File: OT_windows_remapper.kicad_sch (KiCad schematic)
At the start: 68 parts, among them J5 ICSP, Q1 BC547, Q10 BC547, Q2 BC547, Q3 BC547, Q4 BC558, Q5 BC558, Q6 BC558, Q7 BC558, Q8 BC558, Q9 BC558, U1 ATmega328P-P, U2 L7805, Y1 16M

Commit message: First routing
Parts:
- removed C7: 100n, Capacitor_THT:C_Rect_L7.0mm_W2.5mm_P5.00mm, symbol Device:C
- removed J15, J2: (no value), symbol Connector:Screw_Terminal_01x02
- removed J16: (no value), symbol Connector:Screw_Terminal_01x03
- added J15, J2, J4: 12Vdc, Connector_Wire:SolderWire-2sqmm_1x01_D2mm_OD3.9mm, symbol Connector:Screw_Terminal_01x01
- added J16: (no value), Connector_Wire:SolderWire-0.75sqmm_1x01_D1.25mm_OD2.3mm, symbol Connector:Screw_Terminal_01x01
- added J17: GND, Connector_Wire:SolderWire-0.75sqmm_1x01_D1.25mm_OD2.3mm, symbol Connector:Screw_Terminal_01x01
- added J18, J19: (no value), Connector_Wire:SolderWire-2sqmm_1x01_D2mm_OD3.9mm, symbol Connector:Screw_Terminal_01x01
- D1, D2, D3, D4, D5, D6, D7: footprint (none) -> Diode_THT:D_DO-41_SOD81_P2.54mm_Vertical_KathodeUp
- J1: value (none) -> Vcc_in
- J10: value (none) -> Down_IN; footprint (none) -> Connector_Wire:SolderWire-0.75sqmm_1x01_D1.25mm_OD2.3mm
- J11: value (none) -> Up_IN; footprint (none) -> Connector_Wire:SolderWire-0.75sqmm_1x01_D1.25mm_OD2.3mm
- J12: value (none) -> Up_REM; footprint (none) -> Connector_Wire:SolderWire-0.75sqmm_1x01_D1.25mm_OD2.3mm
- J13: value (none) -> Down_REM; footprint (none) -> Connector_Wire:SolderWire-0.75sqmm_1x01_D1.25mm_OD2.3mm
- J14: value (none) -> CClose_IN; footprint (none) -> Connector_Wire:SolderWire-0.75sqmm_1x01_D1.25mm_OD2.3mm
- J3: value (none) -> EPSW_aux; footprint (none) -> Connector_Wire:SolderWire-0.75sqmm_1x02_P4.8mm_D1.25mm_OD2.3mm
- J6: value (none) -> Up_OUT; footprint (none) -> Connector_Wire:SolderWire-0.75sqmm_1x01_D1.25mm_OD2.3mm
- J7: value (none) -> Down_OUT; footprint (none) -> Connector_Wire:SolderWire-0.75sqmm_1x01_D1.25mm_OD2.3mm
- J8: value (none) -> Auth_OUT; footprint (none) -> Connector_Wire:SolderWire-0.75sqmm_1x01_D1.25mm_OD2.3mm
- J9: value (none) -> Auth_IN; footprint (none) -> Connector_Wire:SolderWire-0.75sqmm_1x01_D1.25mm_OD2.3mm
- R1, R10, R11, R12, R13, R14, R15, R16, R17, R18, R19, R2, R20, R21, R22, R23, R24, R25, R26, R3, R4, R5, R6, R7, R8, R9: footprint (none) -> Resistor_THT:R_Axial_DIN0207_L6.3mm_D2.5mm_P2.54mm_Vertical
- U2: footprint Package_TO_SOT_THT:TO-220-3_Horizontal_TabDown -> (none)
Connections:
- net GND: now also J5.1 (Pin_1), J16.1 (Pin_1), J17.1 (Pin_1), J18.1 (Pin_1), J19.1 (Pin_1); no longer J5.5 (Pin_5)
- net at C4.1, C5.1, J3.2 (Pin_2)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: no longer C6.1
- net at Q7.1 (C), R22.1: now also U1.5 (PD3); no longer U1.13 (PD7)
- net at Q5.1 (C), R20.1: now also U1.14 (PB0); no longer U1.24 (PC1)
- net at Q6.1 (C), R21.1: now also U1.15 (PB1); no longer U1.23 (PC0)
- net at U1.1 (~{RESET}/PC6): now also J5.5 (Pin_5); no longer J5.1 (Pin_1)
- net at J5.2 (Pin_2), U1.17 (PB3): no longer R25.1
- net at R13.1: now also U1.4 (PD2); no longer U1.14 (PB0)
- net at R12.1: now also U1.3 (PD1); no longer U1.15 (PB1)
- net at U1.16 (PB2): now also R25.1; no longer R11.1
- net at U1.2 (PD0): now also R11.1
- net at Q4.1 (C), R19.1: now also U1.6 (PD4); no longer U1.25 (PC2)
- net at C3.1, J1.1 (Pin_1), U2.1 (IN): now also C6.1
- new net: J15.1 (Pin_1), J2.1 (Pin_1), J4.1 (Pin_1)
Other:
- moved on the sheet: C6, U2

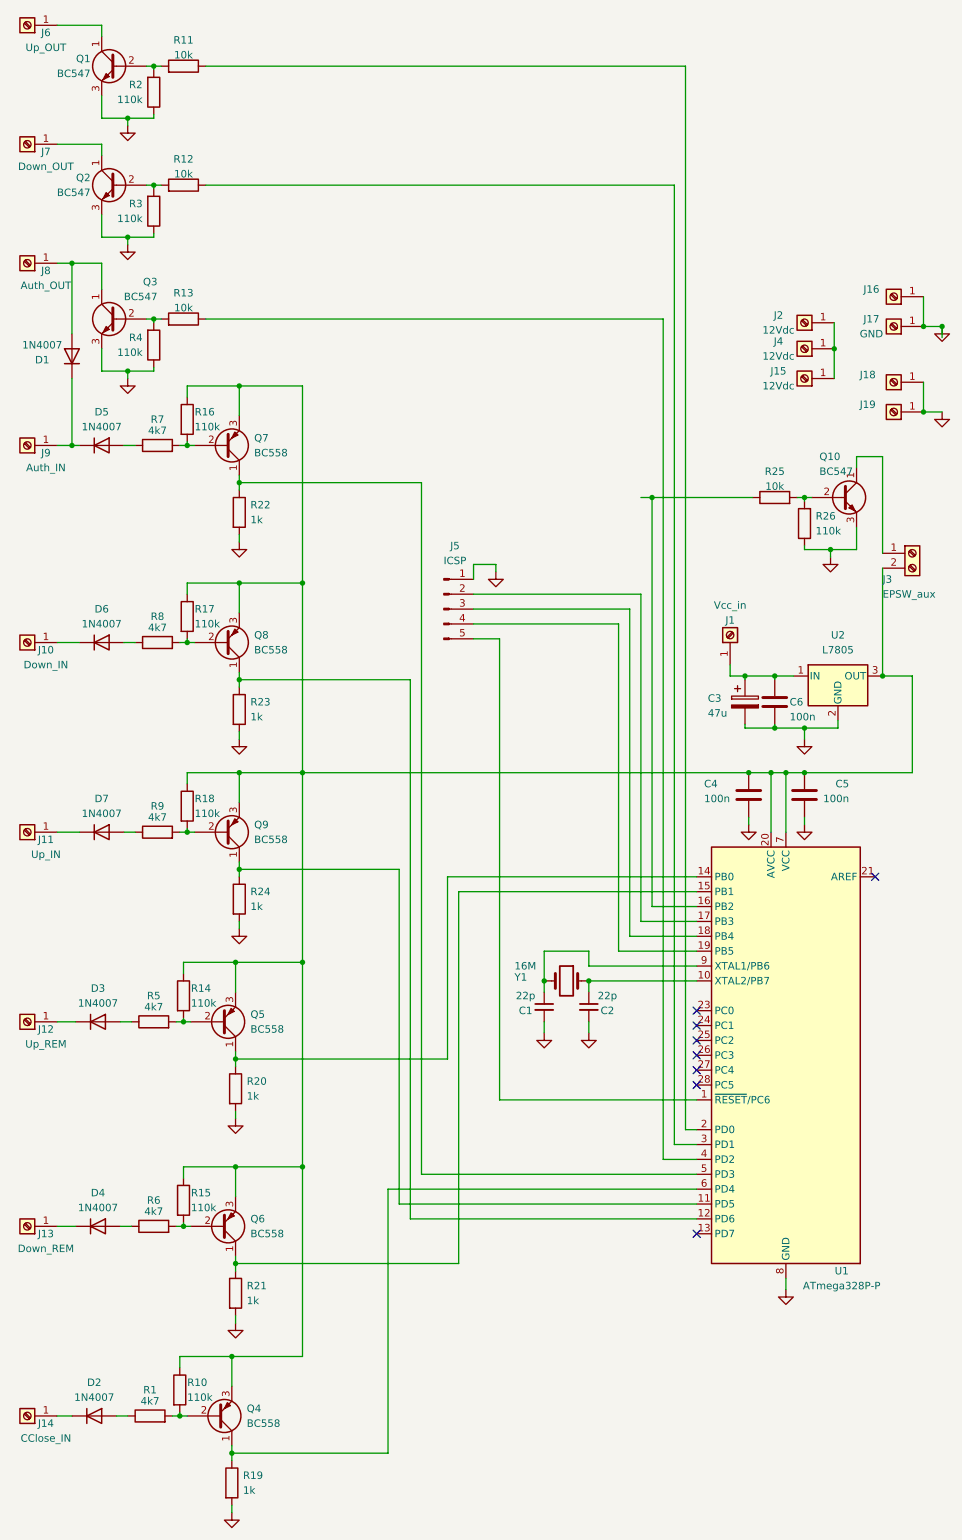
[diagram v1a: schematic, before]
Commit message: Included 12 V pullups resistors on board
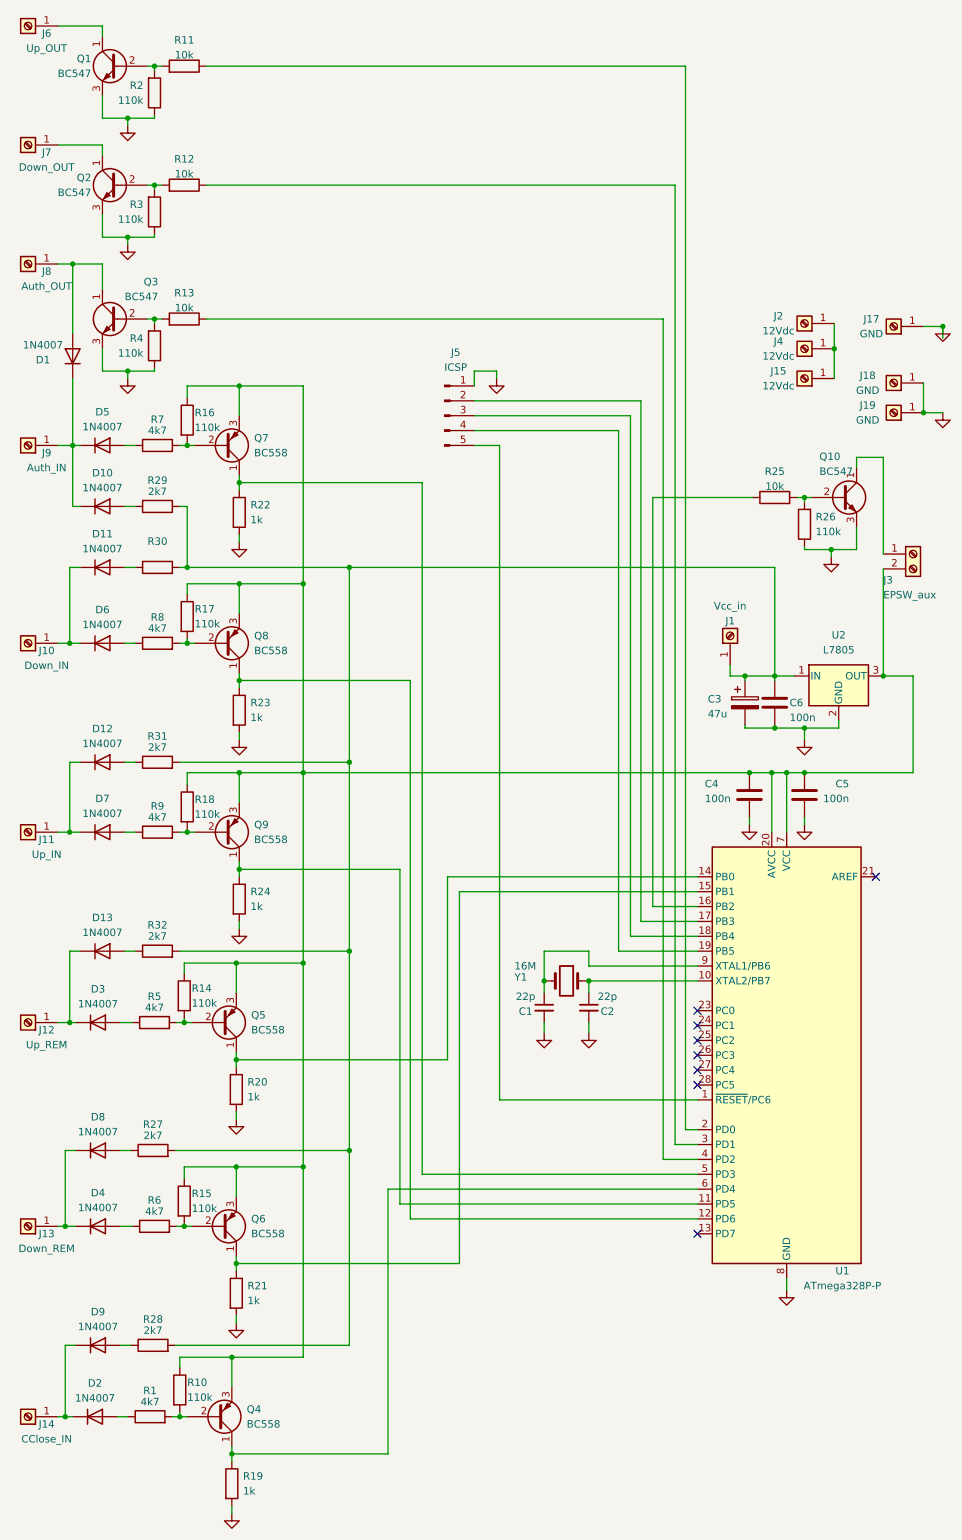
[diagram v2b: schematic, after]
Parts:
- removed J16: (no value), Connector_Wire:SolderWire-0.75sqmm_1x01_D1.25mm_OD2.3mm, symbol Connector:Screw_Terminal_01x01
- added D10, D11, D12, D13, D8, D9: 1N4007, Diode_THT:D_DO-41_SOD81_P2.54mm_Vertical_KathodeUp, symbol Diode:1N4007
- added R27, R28, R29, R31, R32: 2k7, Resistor_THT:R_Axial_DIN0207_L6.3mm_D2.5mm_P2.54mm_Vertical, symbol Device:R
- added R30: (no value), Resistor_THT:R_Axial_DIN0207_L6.3mm_D2.5mm_P2.54mm_Vertical, symbol Device:R
- J18, J19: value (none) -> GND
- U2: footprint (none) -> Package_TO_SOT_THT:TO-220-3_Vertical
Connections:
- net at D1.1 (K), D5.1 (K), J9.1 (Pin_1): now also D10.1 (K)
- net at D3.1 (K), J12.1 (Pin_1): now also D13.1 (K)
- net at D2.1 (K), J14.1 (Pin_1): now also D9.1 (K)
- net at D7.1 (K), J11.1 (Pin_1): now also D12.1 (K)
- net at D6.1 (K), J10.1 (Pin_1): now also D11.1 (K)
- net at C3.1, C6.1, J1.1 (Pin_1)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: now also R27.2, R28.2, R29.2, R30.2, R31.2, R32.2
- net at D4.1 (K), J13.1 (Pin_1): now also D8.1 (K)
- new net: D10.2 (A), R29.1
- new net: D9.2 (A), R28.1
- new net: D12.2 (A), R31.1
- new net: D13.2 (A), R32.1
- new net: D8.2 (A), R27.1
- new net: D11.2 (A), R30.1
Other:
- moved on the sheet: J5
